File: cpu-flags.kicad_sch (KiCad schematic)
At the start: 17 parts, among them U22 74HCT157, U52 74HCT02, U53 74HCT08, U55 74HCT08, U56 74HCT02, U9 74HCT173

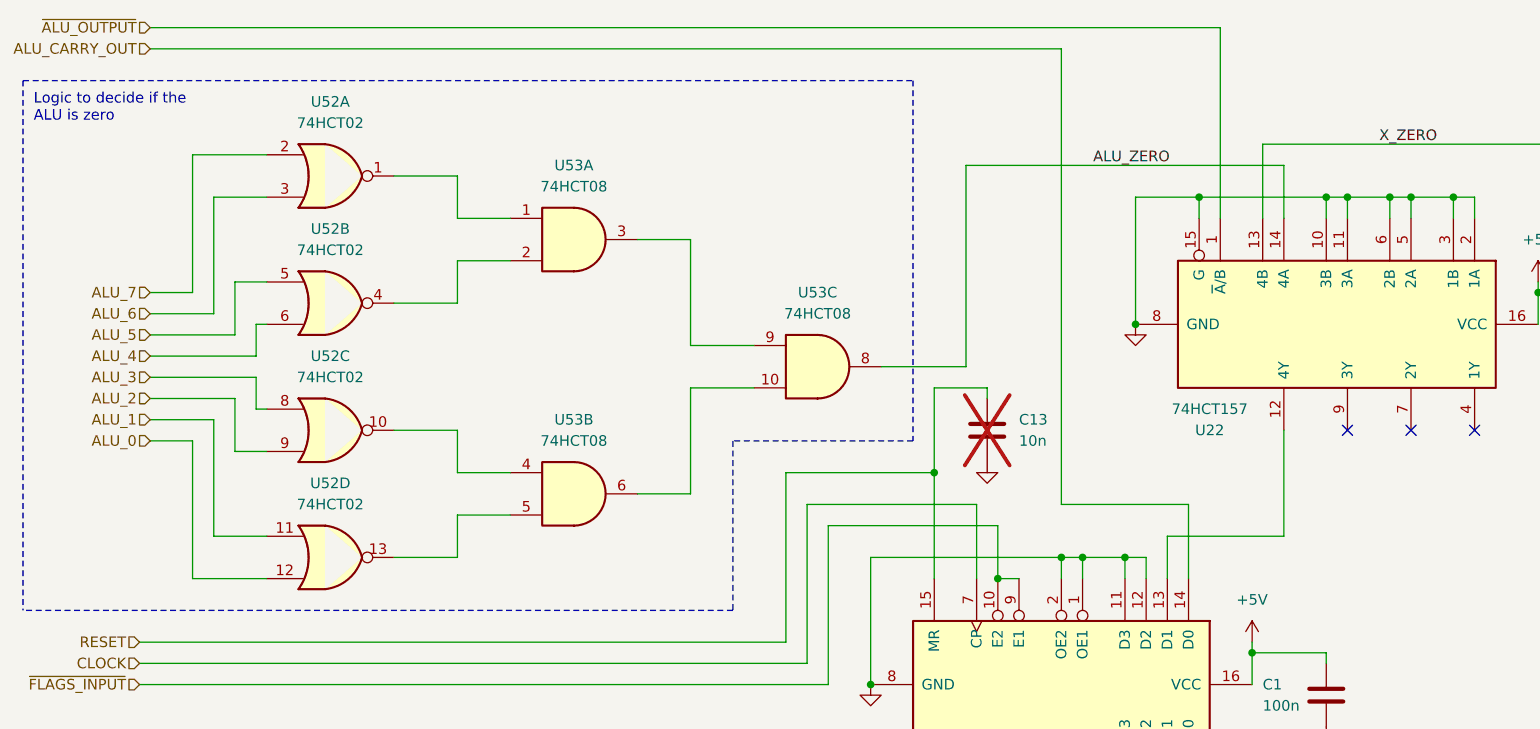
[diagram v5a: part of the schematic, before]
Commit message: alu carry out goes through selector now so we do not set the carry flag when we do incx or decx
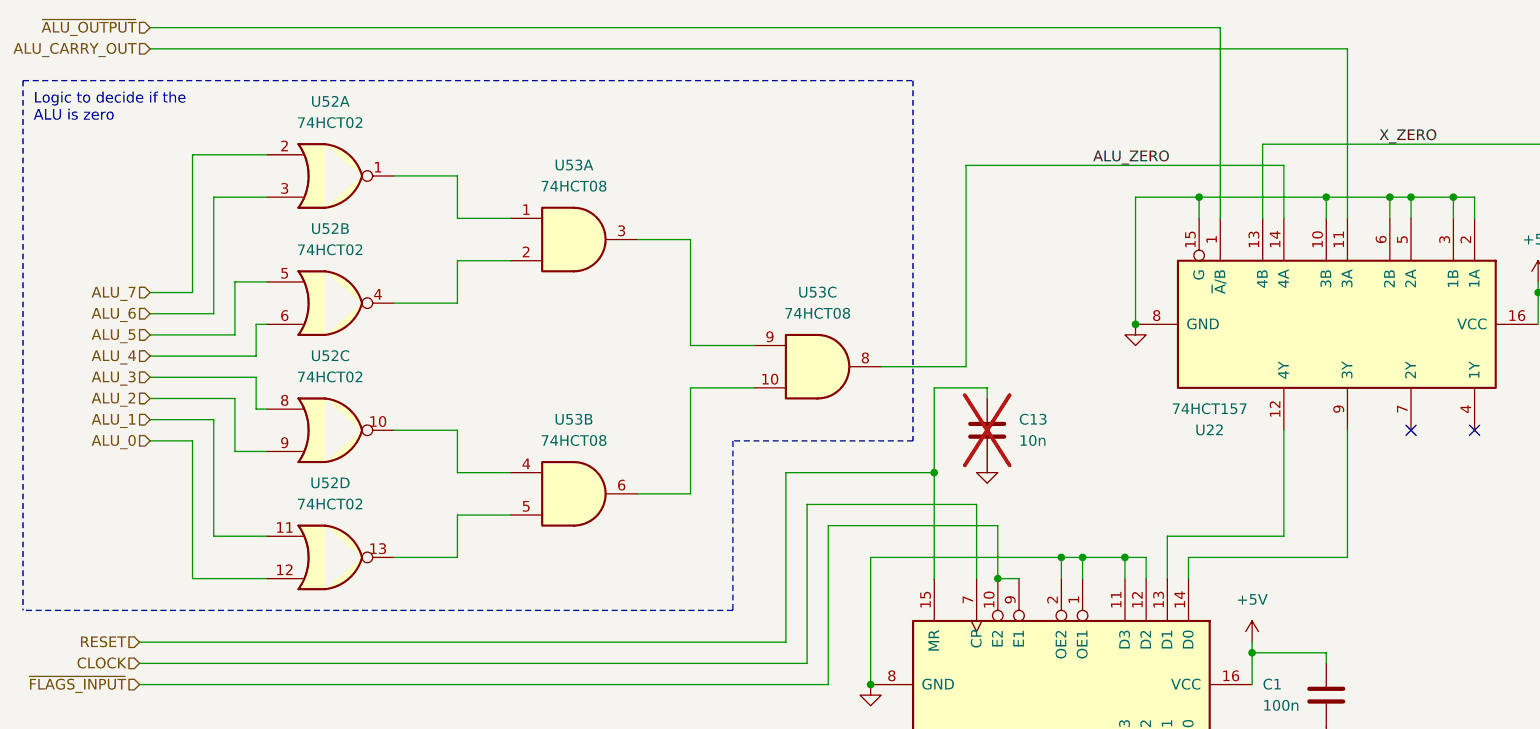
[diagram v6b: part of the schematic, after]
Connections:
- net ALU_CARRY_OUT: now also U22.11 (3A); no longer U9.14 (D0)
- net GND: no longer U22.11 (3A)
- net at U22.9 (3Y): now also U9.14 (D0)
- no-connect marks 7 -> 6
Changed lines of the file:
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@@
     (company "TBR Designs")
-  )
-  (junction (at 176.53 38.1) (diameter 0) (color 0 0 0 0)
   )
   (junction (at 237.49 29.21) (diameter 0) (color 0 0 0 0)
@@
   (no_connect (at 267.97 124.46))
   (no_connect (at 184.15 66.04))
-  (no_connect (at 176.53 66.04))
   (no_connect (at 245.11 124.46))
   (no_connect (at 149.86 109.22))
@@
     (stroke (width 0) (type default))
   )
+  (wire (pts (xy 176.53 66.04) (xy 176.53 81.28))
+    (stroke (width 0) (type default))
+  )
   (wire (pts (xy 265.43 26.67) (xy 265.43 29.21))
     (stroke (width 0) (type default))
@@
     (stroke (width 0) (type default))
   )
-  (wire (pts (xy 181.61 38.1) (xy 176.53 38.1))
+  (wire (pts (xy 173.99 38.1) (xy 181.61 38.1))
     (stroke (width 0) (type default))
   )
@@
     (stroke (width 0) (type default))
   )
-  (wire (pts (xy 176.53 38.1) (xy 176.53 40.64))
-    (stroke (width 0) (type default))
-  )
   (wire (pts (xy 97.79 149.86) (xy 105.41 149.86))
     (stroke (width 0) (type default))
@@
     (stroke (width 0) (type default) (color 255 0 0 1))
   )
-  (wire (pts (xy 176.53 38.1) (xy 173.99 38.1))
-    (stroke (width 0) (type default))
-  )
   (wire (pts (xy 40.64 172.72) (xy 46.99 172.72))
     (stroke (width 0) (type default))
@@
     (stroke (width 0) (type default))
   )
-  (wire (pts (xy 142.24 74.93) (xy 157.48 74.93))
-    (stroke (width 0) (type default))
-  )
   (wire (pts (xy 119.38 81.28) (xy 119.38 96.52))
     (stroke (width 0) (type default))
@@
     (stroke (width 0) (type default))
   )
+  (wire (pts (xy 176.53 20.32) (xy 176.53 40.64))
+    (stroke (width 0) (type default))
+  )
   (wire (pts (xy 97.79 154.94) (xy 105.41 154.94))
     (stroke (width 0) (type default))
@@
     (stroke (width 0) (type default))
   )
+  (wire (pts (xy 157.48 83.82) (xy 157.48 81.28))
+    (stroke (width 0) (type default))
+  )
   (wire (pts (xy 109.22 111.76) (xy 109.22 115.57))
     (stroke (width 0) (type default))
@@
     (stroke (width 0) (type default))
   )
-  (wire (pts (xy 157.48 74.93) (xy 157.48 83.82))
-    (stroke (width 0) (type default))
-  )
   (wire (pts (xy 121.92 115.57) (xy 121.92 114.3))
     (stroke (width 0) (type default))
@@
     (stroke (width 0) (type default))
   )
+  (wire (pts (xy 157.48 81.28) (xy 176.53 81.28))
+    (stroke (width 0) (type default))
+  )
   (wire (pts (xy 38.1 83.82) (xy 46.99 83.82))
     (stroke (width 0) (type default))
@@
     (stroke (width 0) (type default) (color 255 0 0 1))
   )
-  (wire (pts (xy 33.02 20.32) (xy 142.24 20.32))
-    (stroke (width 0) (type default))
-  )
   (wire (pts (xy 265.43 67.31) (xy 265.43 69.85))
     (stroke (width 0) (type default))
@@
     (stroke (width 0) (type dash))
   )
+  (wire (pts (xy 33.02 20.32) (xy 176.53 20.32))
+    (stroke (width 0) (type default))
+  )
   (wire (pts (xy 115.57 130.81) (xy 121.92 130.81))
     (stroke (width 0) (type default))
@@
     (stroke (width 0) (type default))
   )
-  (wire (pts (xy 142.24 20.32) (xy 142.24 74.93))
-    (stroke (width 0) (type default))
-  )

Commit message: kicad update
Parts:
- D105, D106: footprint LED_THT:LED_D5.0mm -> 01_my_library:LED_D5.0mm
- renumbered C2 to C66, C2 to C67, C1 to C68, C13 to C69, C2 to C70, C2 to C71, C1 to C72, U22 to U54, U9 to U57
